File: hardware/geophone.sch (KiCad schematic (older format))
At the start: 11 parts

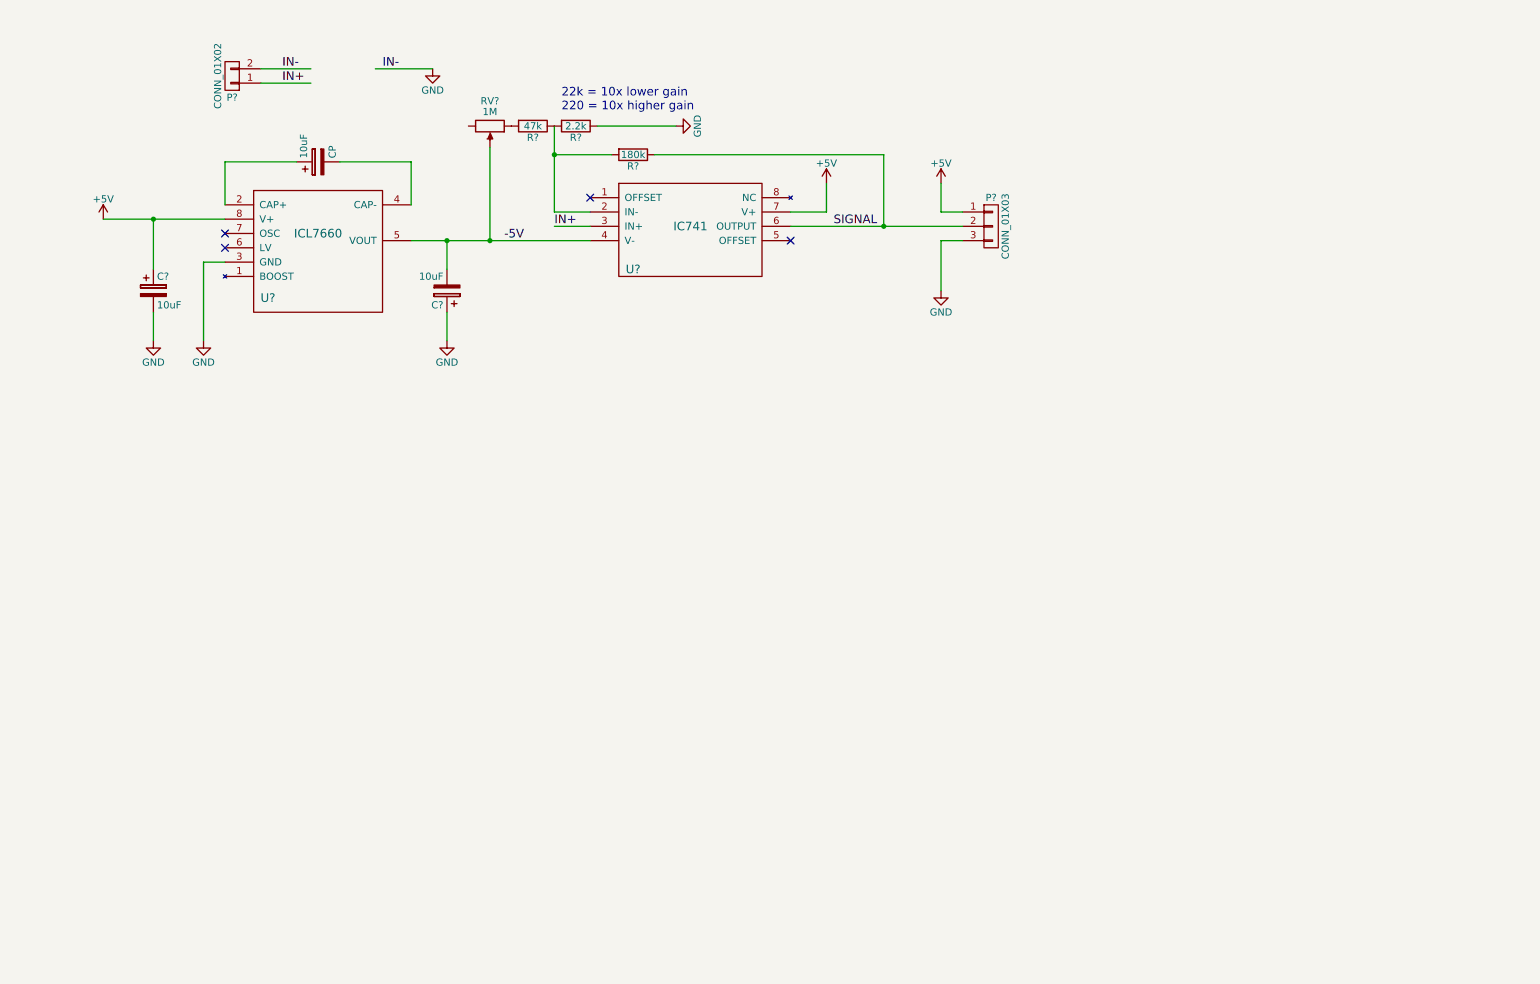
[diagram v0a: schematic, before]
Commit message: First pass at the PCB with XYZ geophones.
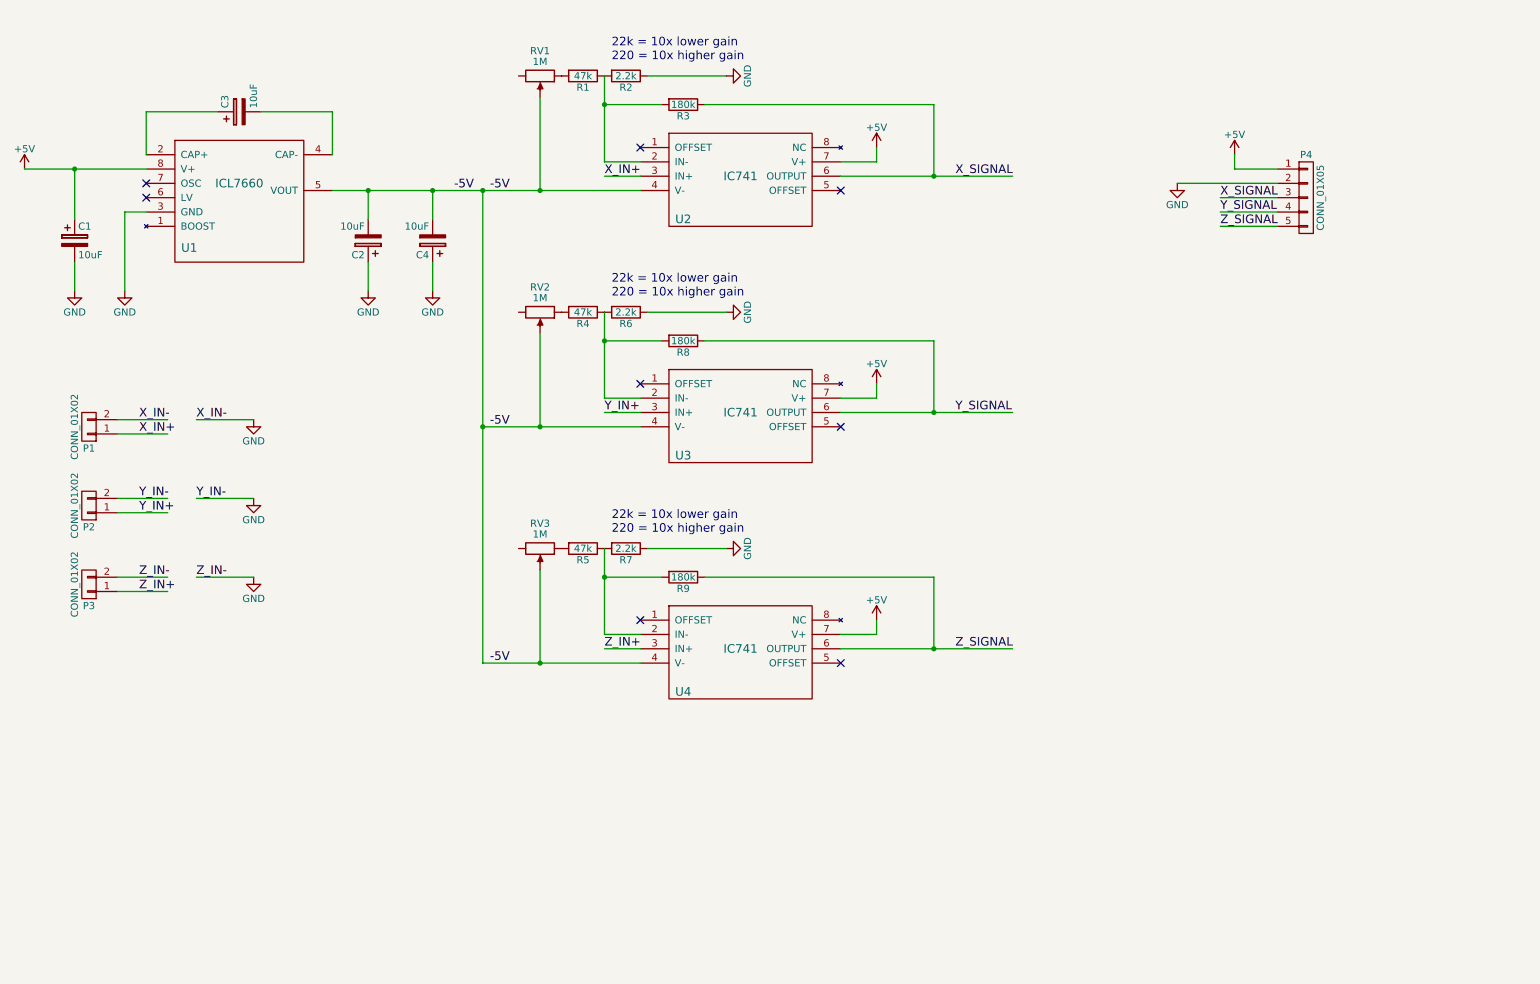
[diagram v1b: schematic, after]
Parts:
- removed P?: CONN_01X03, symbol CONN_01X03
- added C4: 10uF, Capacitors_ThroughHole:CP_Radial_D10.0mm_P5.00mm_P7.50mm, symbol CP
- added P2, P3: CONN_01X02, Socket_Strips:Socket_Strip_Straight_1x02, symbol CONN_01X02
- added P4: CONN_01X05, Socket_Strips:Socket_Strip_Straight_1x05, symbol CONN_01X05
- added R4, R5: 47k, Resistors_ThroughHole:R_Axial_DIN0207_L6.3mm_D2.5mm_P10.16mm_Horizontal, symbol R
- added R6, R7: 2.2k, Resistors_ThroughHole:R_Axial_DIN0207_L6.3mm_D2.5mm_P10.16mm_Horizontal, symbol R
- added R8, R9: 180k, Resistors_ThroughHole:R_Axial_DIN0207_L6.3mm_D2.5mm_P10.16mm_Horizontal, symbol R
- added RV2, RV3: 1M, hardware:POT, symbol POT
- added U3, U4: IC741, Housings_DIP:DIP-8_W7.62mm_LongPads, symbol IC741
- C1, C2: renamed from C?; footprint (none) -> Capacitors_ThroughHole:CP_Radial_D10.0mm_P5.00mm_P7.50mm; SPN (none) -> 493-7383-1-ND
- C3: renamed from 10uF; value CP -> 10uF; footprint (none) -> Capacitors_ThroughHole:CP_Radial_D10.0mm_P5.00mm_P7.50mm; SPN (none) -> 493-7383-1-ND
- P1: renamed from P?; footprint (none) -> Socket_Strips:Socket_Strip_Straight_1x02
- R1: renamed from R?; footprint (none) -> Resistors_ThroughHole:R_Axial_DIN0207_L6.3mm_D2.5mm_P10.16mm_Horizontal; SPN (none) -> CF14JT47K0CT-ND
- R2: renamed from R?; footprint (none) -> Resistors_ThroughHole:R_Axial_DIN0207_L6.3mm_D2.5mm_P10.16mm_Horizontal; SPN (none) -> 2.2KQBK-ND
- R3: renamed from R?; footprint (none) -> Resistors_ThroughHole:R_Axial_DIN0207_L6.3mm_D2.5mm_P10.16mm_Horizontal; SPN (none) -> CF14JT180KCT-ND
- RV1: renamed from RV?; footprint (none) -> hardware:POT; SPN (none) -> 3310Y-001-105L-ND
- U1: renamed from U?; footprint (none) -> Housings_DIP:DIP-8_W7.62mm_LongPads; SPN (none) -> ICL7660SIPAZ-ND
- U2: renamed from U?; footprint (none) -> Housings_DIP:DIP-8_W7.62mm_LongPads; SPN (none) -> LM741CNNS/NOPB-ND
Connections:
- net labels added: X_IN+, X_IN-, X_SIGNAL, Y_IN+, Y_IN-, Y_SIGNAL, Z_IN+, Z_IN-, Z_SIGNAL
- net labels removed: IN+, IN-, SIGNAL
- wire segments 30 -> 65
- no-connect marks 4 -> 8
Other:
- moved on the sheet: C1, C2, C3, P1, R1, R2, R3, RV1, U1, U2

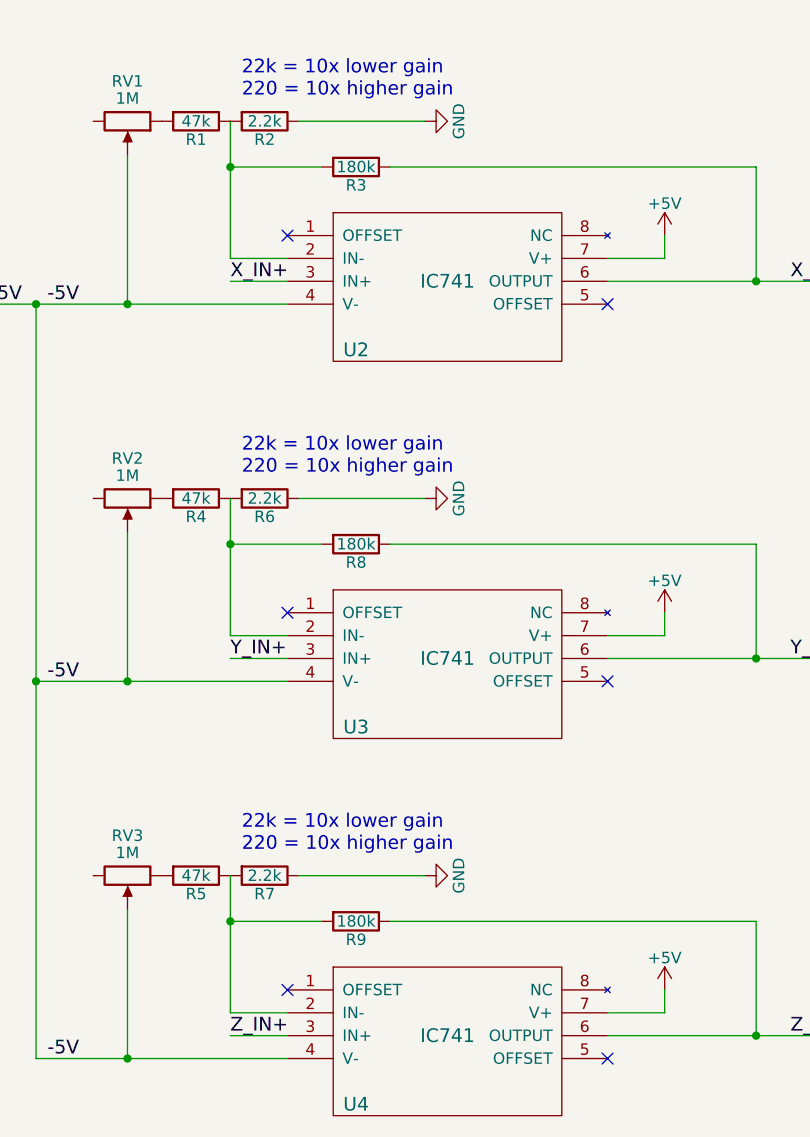
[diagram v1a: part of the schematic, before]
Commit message: Adding jumpers to make changing gain R a little easier.
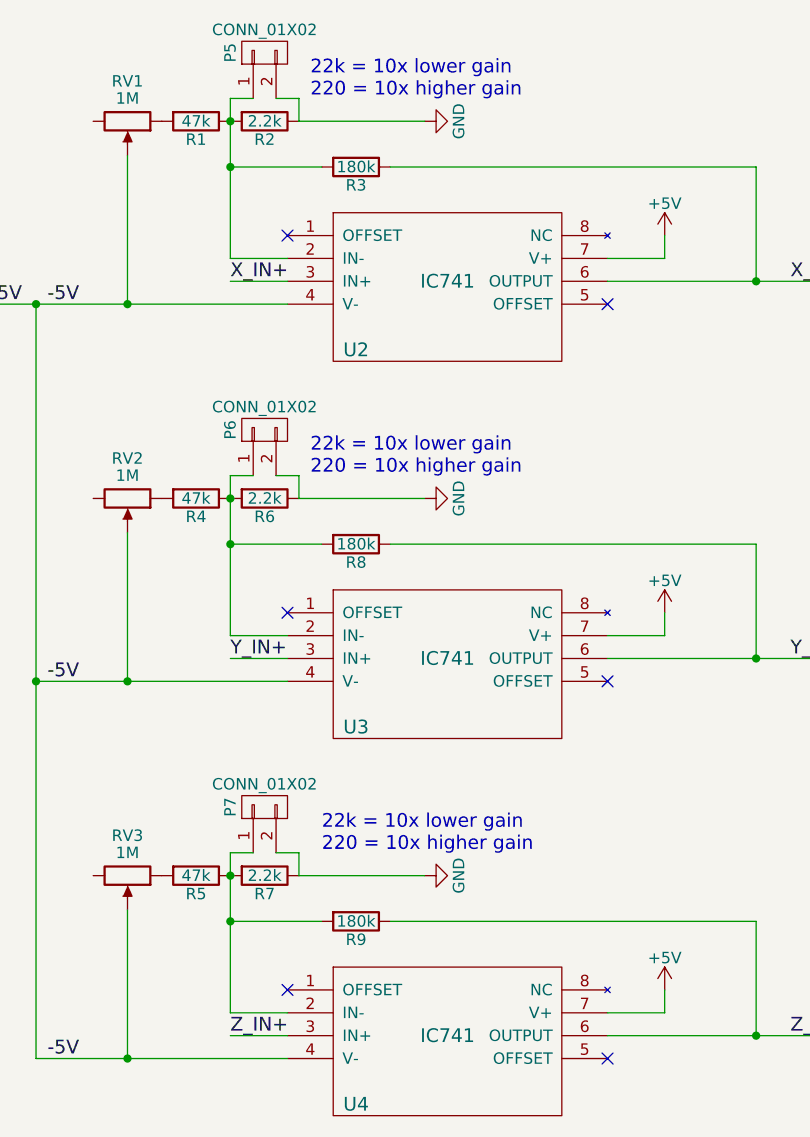
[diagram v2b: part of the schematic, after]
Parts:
- added P5, P6, P7: CONN_01X02, Socket_Strips:Socket_Strip_Straight_1x02, symbol CONN_01X02
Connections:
- wire segments 65 -> 74
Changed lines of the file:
@@
 	4650 1650 4900 1650
 Wire Wire Line
-	4650 1050 4650 1650
+	4650 950  4650 1650
 Wire Wire Line
 	5050 1250 4650 1250
@@
 Text Label 3850 1850 0    60   ~ 0
 -5V
-Text Notes 4700 950  0    60   ~ 0
+Text Notes 5000 950  0    60   ~ 0
 22k = 10x lower gain\n220 = 10x higher gain
 $Comp
@@
 	4650 3300 4900 3300
 Wire Wire Line
-	4650 2700 4650 3300
+	4650 2600 4650 3300
 Wire Wire Line
 	5050 2900 4650 2900
@@
 Text Label 3850 3500 0    60   ~ 0
 -5V
-Text Notes 4700 2600 0    60   ~ 0
+Text Notes 5000 2600 0    60   ~ 0
 22k = 10x lower gain\n220 = 10x higher gain
 $Comp
@@
 	4650 4950 4900 4950
 Wire Wire Line
-	4650 4350 4650 4950
+	4650 4250 4650 4950
 Wire Wire Line
 	5050 4550 4650 4550
@@
 Text Label 3850 5150 0    60   ~ 0
 -5V
-Text Notes 4700 4250 0    60   ~ 0
+Text Notes 5050 4250 0    60   ~ 0
 22k = 10x lower gain\n220 = 10x higher gain
 Wire Wire Line
@@
 Text Label 3600 1850 0    60   ~ 0
 -5V
+$Comp
+L CONN_01X02 P5
+U 1 1 58911DFB
+P 4800 750
+F 0 "P5" H 4800 900 50  0000 C CNN
+F 1 "CONN_01X02" V 4900 750 50  0000 C CNN
+F 2 "Socket_Strips:Socket_Strip_Straight_1x02" H 4800 750 50  0001 C CNN
+F 3 "" H 4800 750 50  0000 C CNN
+	1    4800 750
+	0    -1   -1   0
+$EndComp
+Wire Wire Line
+	4850 950  4950 950
+Wire Wire Line
+	4950 950  4950 1050
+Wire Wire Line
+	4750 950  4650 950
+Connection ~ 4650 1050
+$Comp
+L CONN_01X02 P6
+U 1 1 589122FA
+P 4800 2400
+F 0 "P6" H 4800 2550 50  0000 C CNN
+F 1 "CONN_01X02" V 4900 2400 50  0000 C CNN
+F 2 "Socket_Strips:Socket_Strip_Straight_1x02" H 4800 2400 50  0001 C CNN
+F 3 "" H 4800 2400 50  0000 C CNN
+	1    4800 2400
+	0    -1   -1   0
+$EndComp
+$Comp
+L CONN_01X02 P7
+U 1 1 5891236E
+P 4800 4050
+F 0 "P7" H 4800 4200 50  0000 C CNN
+F 1 "CONN_01X02" V 4900 4050 50  0000 C CNN
+F 2 "Socket_Strips:Socket_Strip_Straight_1x02" H 4800 4050 50  0001 C CNN
+F 3 "" H 4800 4050 50  0000 C CNN
+	1    4800 4050
+	0    -1   -1   0
+$EndComp
+Wire Wire Line
+	4650 4250 4750 4250
+Connection ~ 4650 4350
+Wire Wire Line
+	4850 4250 4950 4250
+Wire Wire Line
+	4950 4250 4950 4350
+Wire Wire Line
+	4750 2600 4650 2600
+Connection ~ 4650 2700
+Wire Wire Line
+	4850 2600 4950 2600
+Wire Wire Line
+	4950 2600 4950 2700
 $EndSCHEMATC
